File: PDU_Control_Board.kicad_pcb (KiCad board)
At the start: 4 copper layers, 171.4 x 233.5 mm, 220 parts, among them J1 Current_Sensor, J10 Precharge_2, J11 Shunt_2, J12 VIN_Enable, J13 1-776087-1, J14 Resistor, J15 GNDPWR, J16 VDC_OUT1_Relay, J17 VDC_OUT2_Rela, J2 Shunt_1, J20 VDC_IN, J21 VDC_OUT1, J22 VDC_OUT2, J3 SWD, J4 Precharge_1, J5 Precharge_2, J6 Shunt_2, J7 VIN_Enable, J8 Precharge_1, J9 Shunt_1, Q1 BSP75N, Q10 BC817, Q2 BSP75N, Q3 BSP75N, Q4 BSP75N, Q5 BSP75N, Q6 BC817, Q7 BC817, Q8 BC817, Q9 BC817, U1 LMV321, U2 APM32F405xG, U3 LMV321, U4 LMV321, U5 LMV321, U6 LMV321, Y2 X322516MOB4SI

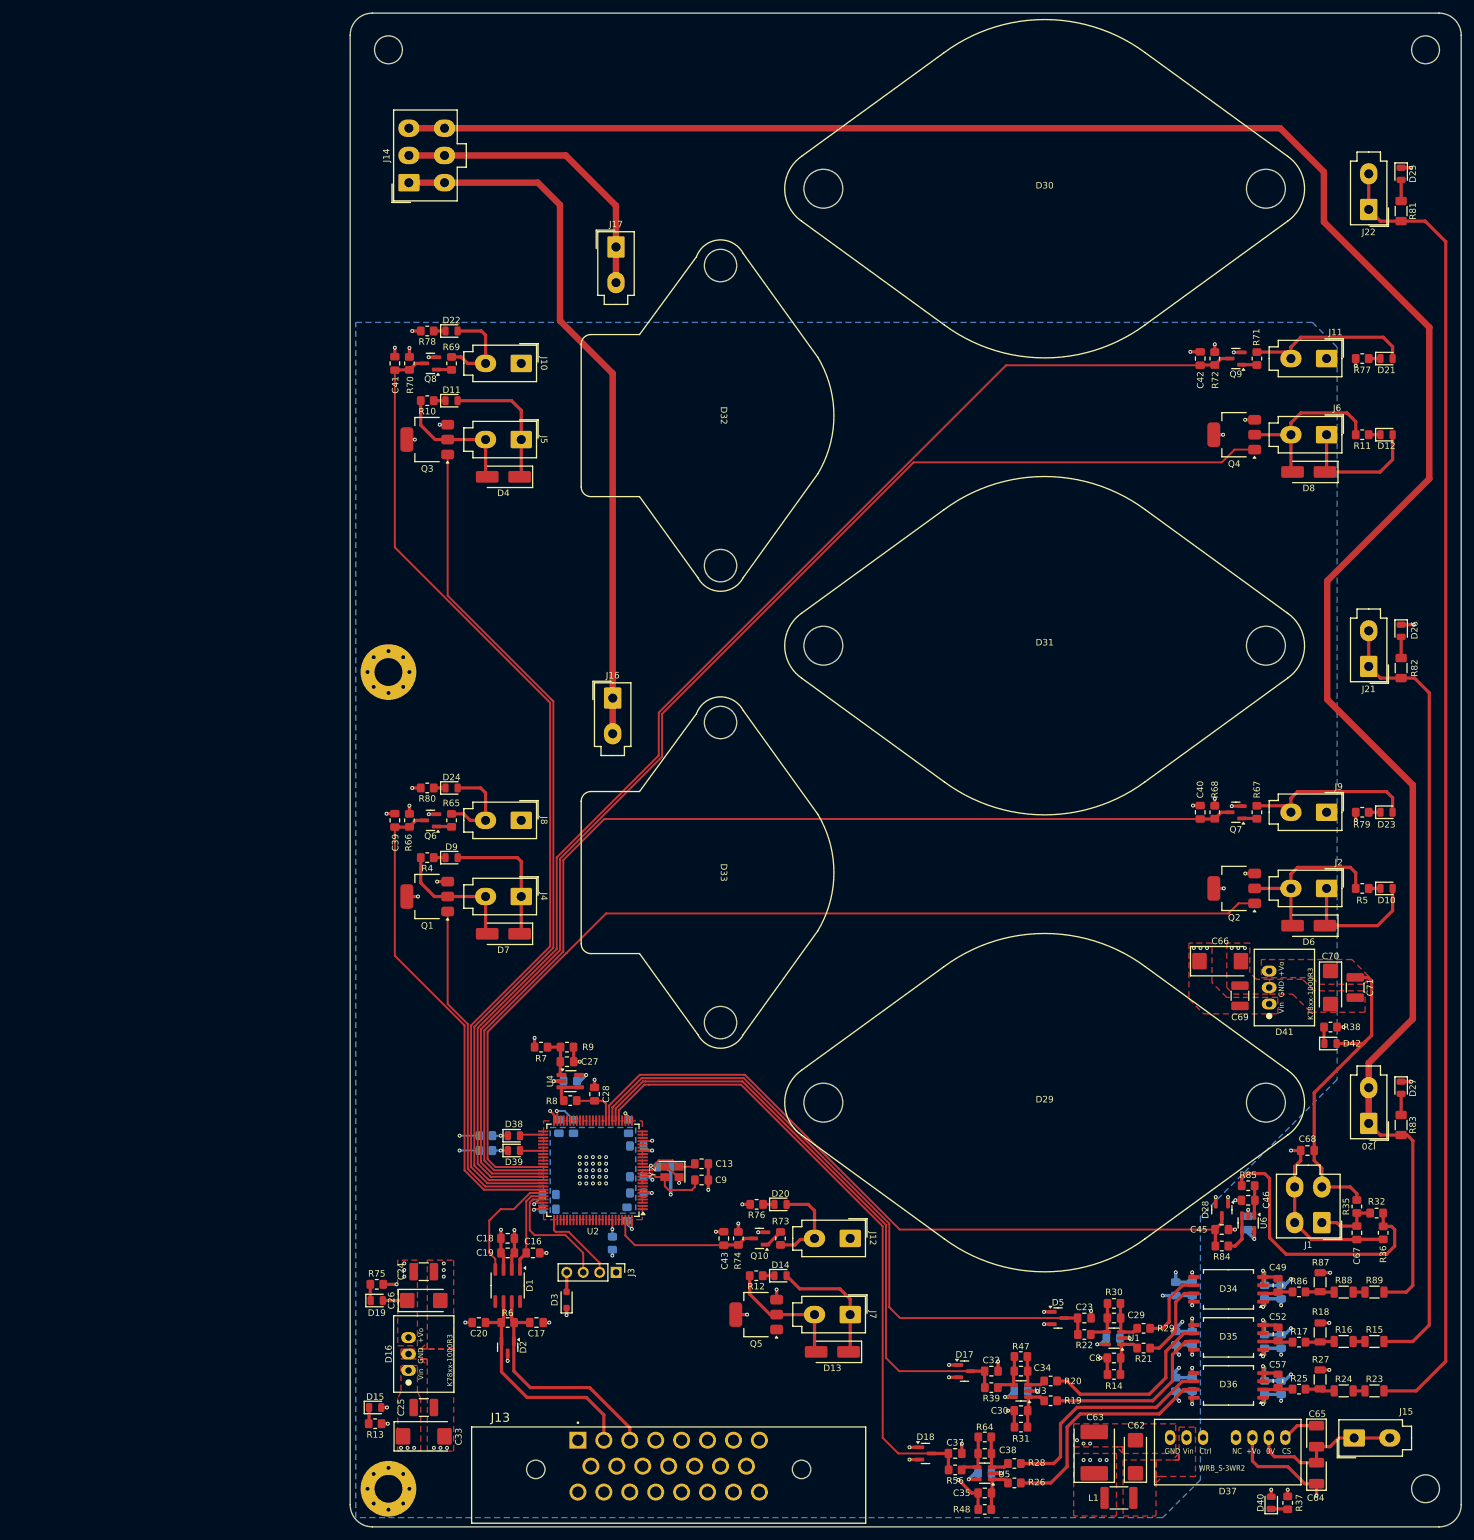
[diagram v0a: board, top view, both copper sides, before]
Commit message: VER2.0: добавил зарядные резисторы
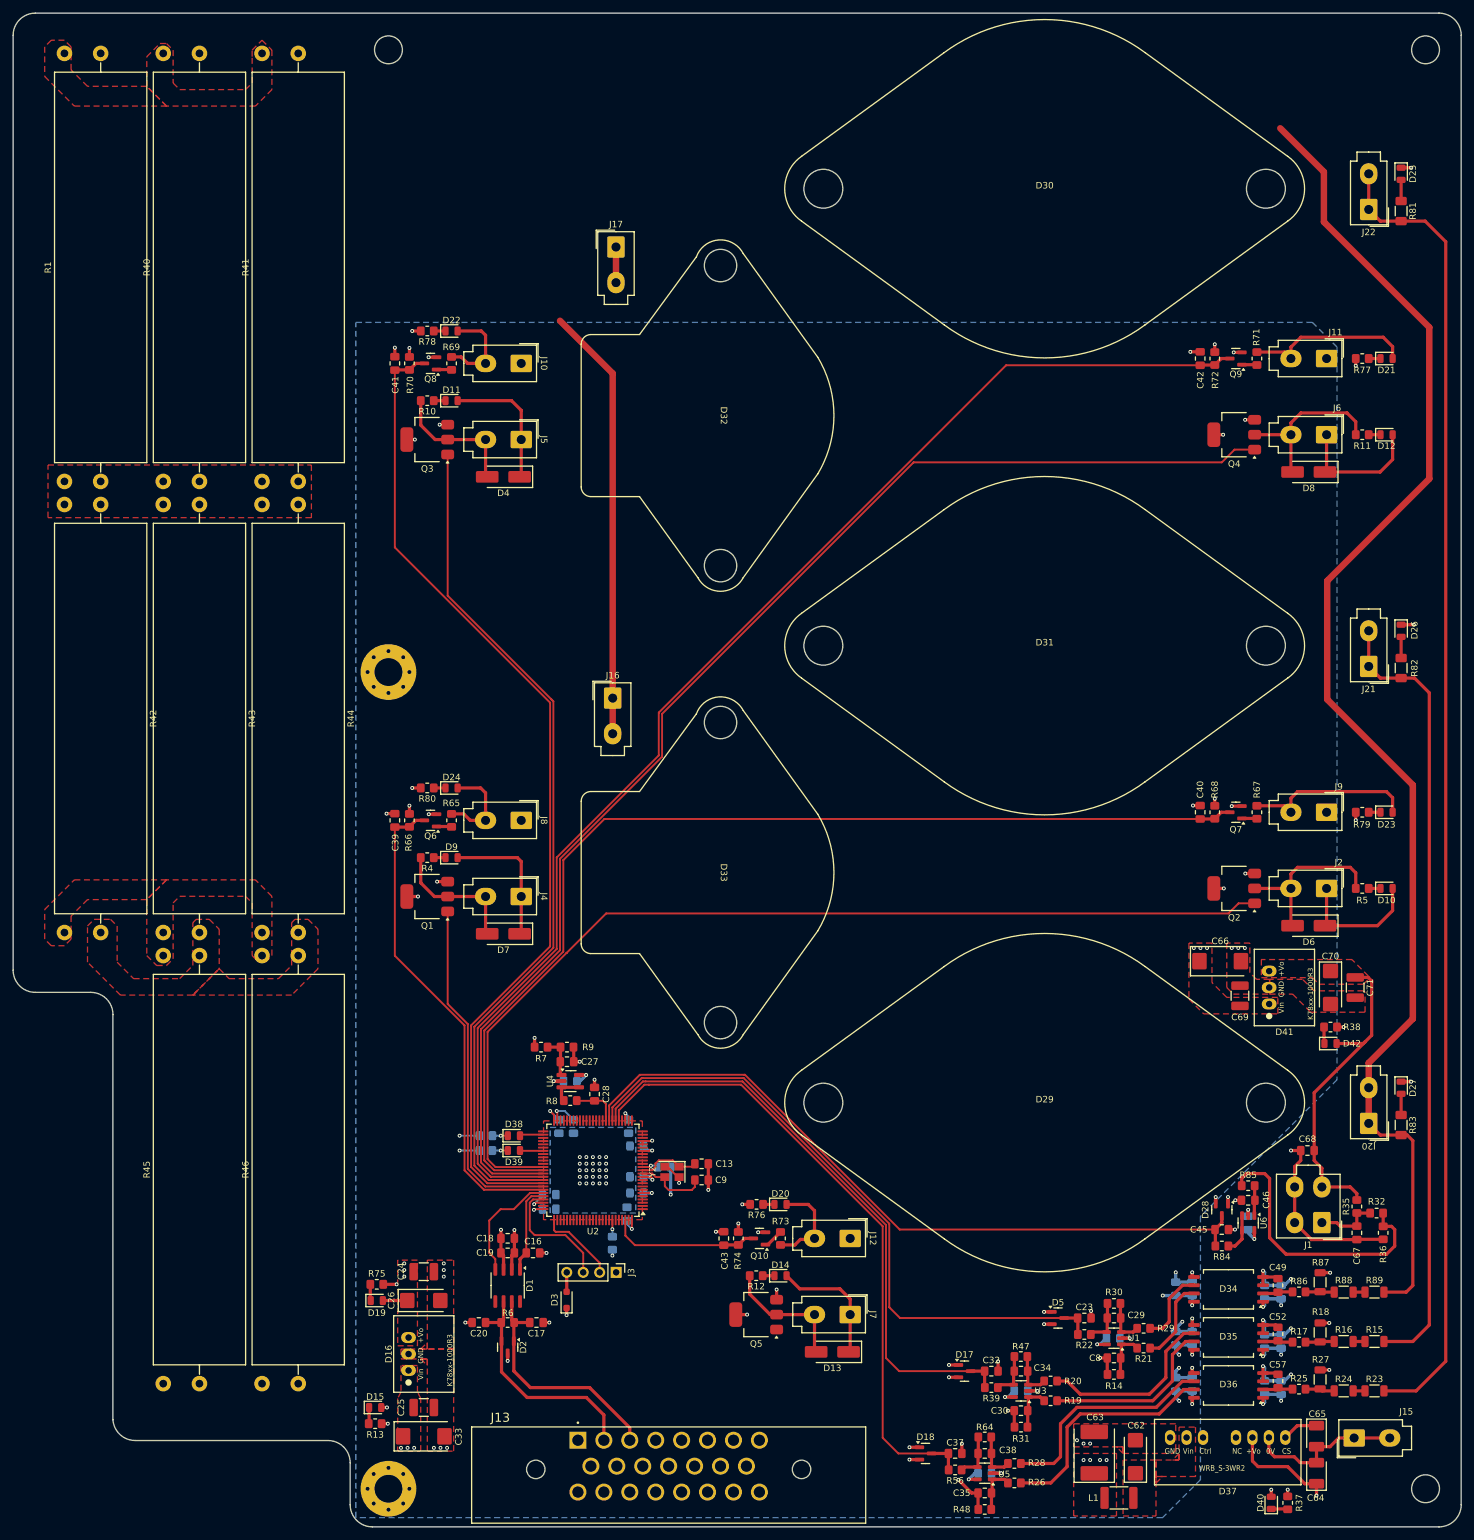
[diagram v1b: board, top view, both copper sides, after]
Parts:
- removed J14: Resistor, Connector_Molex:Molex_Mini-Fit_Jr_5566-06A_2x03_P4.20mm_Vertical
- added R1: 10k, Resistor_THT:R_Axial_Power_L60.0mm_W14.0mm_P66.04mm, F.Cu at (101.6, 164.6)
- added R40: 10k, Resistor_THT:R_Axial_Power_L60.0mm_W14.0mm_P66.04mm, F.Cu at (116.8, 164.6)
- added R41: 10k, Resistor_THT:R_Axial_Power_L60.0mm_W14.0mm_P66.04mm, F.Cu at (132.1, 164.6)
- added R42: 10k, Resistor_THT:R_Axial_Power_L60.0mm_W14.0mm_P66.04mm, F.Cu at (101.6, 168.1)
- added R43: 10k, Resistor_THT:R_Axial_Power_L60.0mm_W14.0mm_P66.04mm, F.Cu at (116.8, 168.1)
- added R44: 10k, Resistor_THT:R_Axial_Power_L60.0mm_W14.0mm_P66.04mm, F.Cu at (132.1, 168.1)
- added R45: 10k, Resistor_THT:R_Axial_Power_L60.0mm_W14.0mm_P66.04mm, F.Cu at (116.8, 303.8)
- added R46: 10k, Resistor_THT:R_Axial_Power_L60.0mm_W14.0mm_P66.04mm, F.Cu at (132.1, 303.8)
- added R49: 10k, Resistor_THT:R_Axial_Power_L60.0mm_W14.0mm_P66.04mm, B.Cu at (96.0, 164.6)
- added R50: 10k, Resistor_THT:R_Axial_Power_L60.0mm_W14.0mm_P66.04mm, B.Cu at (111.3, 164.6)
- added R51: 10k, Resistor_THT:R_Axial_Power_L60.0mm_W14.0mm_P66.04mm, B.Cu at (126.5, 164.6)
- added R52: 10k, Resistor_THT:R_Axial_Power_L60.0mm_W14.0mm_P66.04mm, B.Cu at (96.0, 168.1)
- added R53: 10k, Resistor_THT:R_Axial_Power_L60.0mm_W14.0mm_P66.04mm, B.Cu at (111.3, 168.1)
- added R54: 10k, Resistor_THT:R_Axial_Power_L60.0mm_W14.0mm_P66.04mm, B.Cu at (126.5, 168.1)
- added R55: 10k, Resistor_THT:R_Axial_Power_L60.0mm_W14.0mm_P66.04mm, B.Cu at (111.3, 303.8)
- added R57: 10k, Resistor_THT:R_Axial_Power_L60.0mm_W14.0mm_P66.04mm, B.Cu at (126.5, 303.8)
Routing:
- net VDC_IN: track 347.4 -> 213.0 mm
- net VDC_OUT1_Relay: track 109.7 -> 67.1 mm
- net VDC_OUT2_Relay: track 47.0 -> 5.50 mm
- added copper zone on F.Cu, net VDC_IN
- added copper zone on F.Cu, net VDC_OUT1_Relay
- added copper zone on F.Cu, net VDC_OUT2_Relay
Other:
- board size 171.4 x 233.5 mm -> 223.4 x 233.5 mm

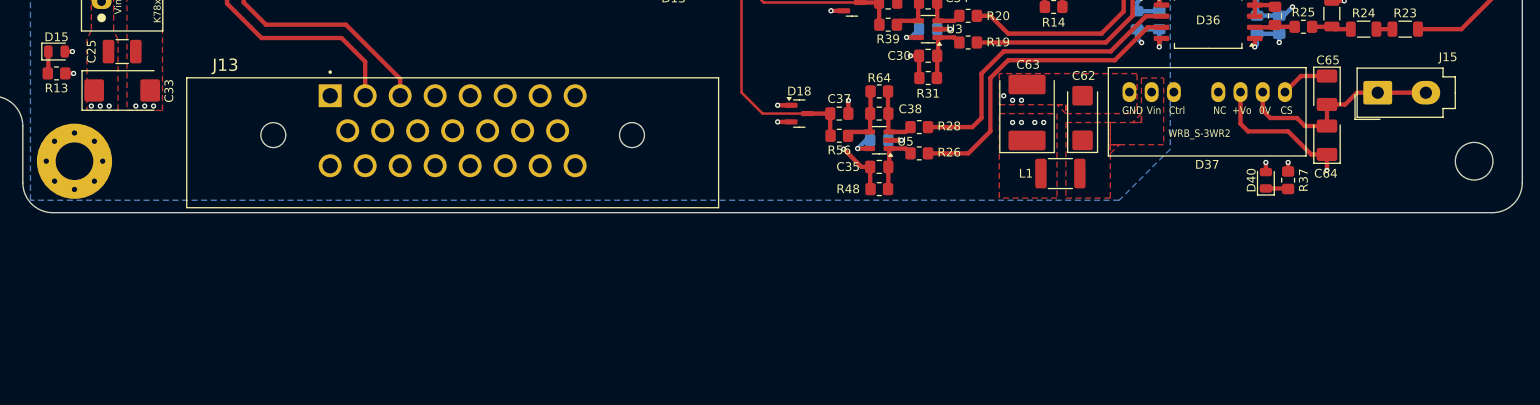
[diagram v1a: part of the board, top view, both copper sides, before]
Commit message: VER2.0: выдвинул разъём вперед платы
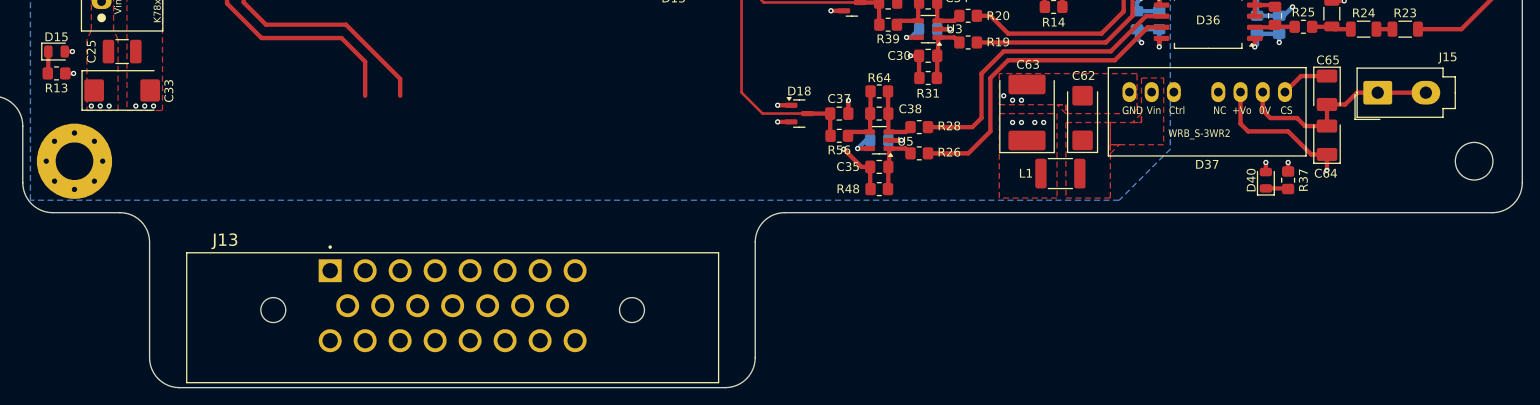
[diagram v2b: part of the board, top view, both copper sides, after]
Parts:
- moved J13 20.0 mm to (175.2, 332.5)
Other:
- board size 223.4 x 233.5 mm -> 223.4 x 253.5 mm
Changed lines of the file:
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@@
 	(footprint "Connector_My:TE_1-776087-1"
 		(layer "F.Cu")
-		(at 175.23 312.5145)
+		(at 175.23 332.5145)
 		(property "Reference" "J13"
 			(at -11.972125 -3.494005 0)
@@
 		(layer "Edge.Cuts")
 	)
+	(gr_arc
+		(start 223.81722 329.2)
+		(mid 224.838654 326.833275)
+		(end 227.23444 325.882)
+		(stroke
+			(width 0.05)
+			(type default)
+		)
+		(layer "Edge.Cuts")
+	)
+	(gr_line
+		(start 154.58278 342.46478)
+		(end 154.58278 329.2)
+		(stroke
+			(width 0.05)
+			(type default)
+		)
+		(layer "Edge.Cuts")
+	)
+	(gr_line
+		(start 220.4 345.882)
+		(end 158 345.882)
+		(stroke
+			(width 0.05)
+			(type default)
+		)
+		(layer "Edge.Cuts")
+	)
 	(gr_line
 		(start 103.49322 246.83444)
@@
 	)
 	(gr_line
-		(start 143.51 325.882)
+		(start 227.23444 325.882)
 		(end 308.086 325.882)
 		(stroke
@@
 		(layer "Edge.Cuts")
 	)
+	(gr_line
+		(start 223.81722 342.46478)
+		(end 223.81722 329.2)
+		(stroke
+			(width 0.05)
+			(type default)
+		)
+		(layer "Edge.Cuts")
+	)
 	(gr_arc
 		(start 308.086 92.34078)
@@
 		(layer "Edge.Cuts")
 	)
+	(gr_arc
+		(start 158 345.882)
+		(mid 155.583665 344.881115)
+		(end 154.58278 342.46478)
+		(stroke
+			(width 0.05)
+			(type default)
+		)
+		(layer "Edge.Cuts")
+	)
+	(gr_line
+		(start 143.51 325.882)
+		(end 151.16556 325.882)
+		(stroke
+			(width 0.05)
+			(type default)
+		)
+		(layer "Edge.Cuts")
+	)
 	(gr_line
 		(start 308.086 92.34078)
@@
 	)
 	(gr_arc
+		(start 223.81722 342.46478)
+		(mid 222.816335 344.881115)
+		(end 220.4 345.882)
+		(stroke
+			(width 0.05)
+			(type default)
+		)
+		(layer "Edge.Cuts")
+	)
+	(gr_arc
 		(start 106.934 312.55878)
 		(mid 104.584195 311.643482)
@@
 		(stroke
 			(width 0.05)
+			(type default)
+		)
+		(layer "Edge.Cuts")
+	)
+	(gr_arc
+		(start 151.16556 325.882)
+		(mid 153.561345 326.833275)
+		(end 154.58278 329.2)
+		(stroke
+			(width 0.05)

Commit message: VER3.0: сделал предварительную расстановку платы
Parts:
- removed D29, D30, D31: EV200, Contactor_My:EV200
- removed D32, D33: SVC100A, Contactor_My:SVC100A
- removed H6: MountingHole_Pad, MountingHole:MountingHole_4.3mm_M4
- removed J15: GNDPWR, Connector_My:Mini-Fit_01x02_Vertical
- removed J16: VDC_OUT1_Relay, Connector_My:Mini-Fit_01x02_Vertical
- removed J17: VDC_OUT2_Rela, Connector_My:Mini-Fit_01x02_Vertical
- removed R1, R40, R41, R42, R43, R44, R45, R46, R49, R50, R51, R52, R53, R54, R55, R57: 10k, Resistor_THT:R_Axial_Power_L60.0mm_W14.0mm_P66.04mm
- added D43: BAT54S, Package_TO_SOT_SMD:SOT-23, F.Cu at (333.2, 229.9)
- H2, H3: footprint MountingHole:MountingHole_4.3mm_M4 -> MountingHole:MountingHole_4.3mm_M4_Pad_Via
- H4: footprint MountingHole:MountingHole_4.3mm_M4_Pad_Via -> MountingHole:MountingHole_4.3mm_M4
- J13: value 1-776087-1 -> To_Main_Connector; footprint Connector_My:TE_1-776087-1 -> Connector_Molex:Molex_Mini-Fit_Jr_5566-04A_2x02_P4.20mm_Vertical
- moved H4 342.2 mm to (452.4, 167.6), turned to -90 degrees
- moved H1 310.4 mm to (452.4, 243.8), turned to -90 degrees
- moved L1 216.8 mm to (450.9, 221.1), turned to 90 degrees
- moved R48 214.5 mm to (430.0, 227.6), turned to 90 degrees
- moved C35 211.1 mm to (427.5, 227.6), turned to 90 degrees
- moved D40 210.3 mm to (451.6, 197.6), turned to 180 degrees
- moved R37 209.8 mm to (451.6, 195.1), turned to 180 degrees
- moved C63 209.1 mm to (443.9, 224.9), turned to 180 degrees
- moved R56 208.6 mm to (423.9, 232.2), turned to -90 degrees
- moved C62 207.1 mm to (444.5, 218.6), turned to 180 degrees
- moved C36 207.0 mm to (424.4, 227.6), turned to 90 degrees
- moved U5 207.0 mm to (424.4, 227.6), turned to -90 degrees
- moved R26 207.0 mm to (425.9, 223.0), turned to -90 degrees
- moved D18 205.6 mm to (417.7, 233.2)
- moved C37 205.2 mm to (421.4, 232.2), turned to 90 degrees
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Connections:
- J13 pad 1: +24V -> CANL
- J13 pad 2: CANL -> +24V
- J13 pad 4: unconnected-(J13-Pad4) -> GND
- J20 pad 2: VDC_IN -> GNDPWR
- J21 pad 2: VDC_OUT1 -> GNDPWR
- J22 pad 2: VDC_OUT2 -> GNDPWR
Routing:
- net VDC_IN: track 213.0 -> 5.75 mm
- net VDC_OUT2: track 203.6 -> 11.2 mm
- net ~{Shunt_2_ON}: track 202.8 -> 15.9 mm
- net Shunt_2: track 199.4 -> 16.2 mm
- net ~{Shunt_1_ON}: track 167.0 -> 14.7 mm
- net Shunt_1: track 155.3 -> 13.8 mm
- net ~{Precharge_2_ON}: track 155.1 -> 17.2 mm
- net Precharge_2: track 133.1 -> 11.5 mm
- net VDC_OUT1: track 122.1 -> 11.2 mm
- net Current_SENSE: track 112.8 -> 2.32 mm
- net VDC_OUT2_SENSE: track 99.3 -> 4.13 mm
- net VDC_IN_SENSE: track 101.1 -> 6.68 mm
- net VDC_OUT1_SENSE: track 93.6 -> 6.55 mm
- net VDC_OUT1_Relay: track 67.1 -> 0.00 mm
- net ~{Precharge_1_ON}: track 75.8 -> 18.4 mm
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- removed copper zone on B.Cu, net +24V
- removed copper zone on In1.Cu, net +3.3V
- removed copper zone on In1.Cu, net +3.3VP
- removed copper zone on F.Cu, net +5V
- removed copper zone on In2.Cu, net GND
- removed copper zone on In2.Cu, net GNDPWR
- removed copper zone on F.Cu, net VDC_IN
- removed copper zone on F.Cu, net VDC_OUT1_Relay
- removed copper zone on F.Cu, net VDC_OUT2_Relay
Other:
- board size 223.4 x 253.5 mm -> 237.7 x 87.4 mm
